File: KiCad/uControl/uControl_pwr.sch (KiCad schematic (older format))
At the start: 30 parts, among them P10 V_IN, P12 UUSB_B, Q1 FDN340P, U1 LP2985-33DBVR, U3 NCP1117ST50T3G, U5 LM358N

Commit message: uControl schematic in progress
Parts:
- removed C15: 1n, c_0805, symbol C
- removed D7: SMBJ5.0CA-TR, diode-DO214AA, symbol DIODE_TRANSIL
- removed F1: nanoSMDC110F, f_1206, symbol FUSE
- removed P12: UUSB_B, USB_B_Micro, symbol UUSB_B
- removed R14: 0E, r_0805, symbol R
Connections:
- net labels removed: USB_IN
- wire segments 89 -> 73
- no-connect marks 3 -> 0
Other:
- note removed: "Bi-directional\nclamping Diode, 5V"
- note removed: "If using Micro USB -B socket, \nDO NOT INSTALL :\nP10, D5, U3\nAND INSTALL\nResistor R14 across pins 2 and 3 of U3\n\nIf using Barrel Socket,\nDO NOT INSTALL :\nP12, F1, D7, C15, R14"
- note removed: "Micro USB-B POWER SOCKET"
- note removed: "Polyswitch resettable fuse\n1.1A Hold, 2.2A Trip 8V max."
- note removed: "TE - 1981568-1\nor\nFCI - 10118193-0001LF"
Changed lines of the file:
@@
-EESchema Schematic File Version 2  date 11/29/2012 6:28:02 PM
+EESchema Schematic File Version 2  date 11/30/2012 11:17:28 AM
 LIBS:uControl
 LIBS:Conn-raspberry
@@
 Sheet 3 5
 Title "uControl"
-Date "29 nov 2012"
+Date "30 nov 2012"
 Rev "1"
 Comp "WyoLum"
@@
 $EndDescr
 Wire Wire Line
-	3575 3925 3575 3400
-Wire Wire Line
-	3575 3400 3300 3400
+	3575 3700 3575 3925
 Wire Notes Line
 	7100 3250 7100 4700
@@
 	7250 4125 7250 4075
 Wire Wire Line
-	7550 4525 7550 4575
+	7550 4575 7550 4525
 Wire Wire Line
 	7550 4575 7250 4575
@@
 Connection ~ 5700 7425
 Wire Wire Line
-	6475 7375 6475 7425
+	6475 7425 6475 7375
 Connection ~ 6350 6400
 Wire Wire Line
-	6475 6425 6475 6400
-Wire Wire Line
-	6475 6400 6300 6400
+	6475 6400 6475 6425
+Wire Wire Line
+	6300 6400 6475 6400
 Connection ~ 5700 5975
 Wire Wire Line
@@
 Wire Notes Line
 	600  5500 600  3250
-Connection ~ 1550 2550
-Wire Wire Line
-	1550 2550 1350 2550
 Connection ~ 5625 5300
 Wire Wire Line
 	5625 5300 5625 5150
-Connection ~ 1550 2200
-Wire Wire Line
-	1550 2200 1350 2200
-Connection ~ 1550 1900
-Wire Wire Line
-	1350 1900 1550 1900
-Wire Wire Line
-	3100 1550 3100 1825
-Connection ~ 3550 1550
-Wire Wire Line
-	3750 1550 1350 1550
-Connection ~ 3100 1550
-Wire Wire Line
-	3550 1550 3550 1450
-Wire Wire Line
-	1350 950  2150 950
 Wire Wire Line
 	7150 6850 7150 6775
@@
 	7425 6775 7425 6725
 Wire Wire Line
-	4150 6275 4150 4375
+	4150 4375 4150 6275
 Wire Wire Line
 	7450 6100 7450 6250
@@
 	2900 7450 2900 7225
 Wire Wire Line
-	4150 4375 4675 4375
+	4675 4375 4150 4375
 Connection ~ 4625 4375
 Wire Wire Line
-	4675 4525 4625 4525
+	4625 4525 4675 4525
 Wire Wire Line
 	1775 5925 3650 5925
@@
 	3025 4250 3025 4350
 Wire Wire Line
-	6400 5300 1800 5300
+	1800 5300 6400 5300
 Connection ~ 1800 3900
 Wire Wire Line
@@
 Connection ~ 4625 5300
 Wire Wire Line
-	2450 4250 2450 4350
+	2450 4350 2450 4250
 Wire Wire Line
 	2450 4350 3850 4350
 Connection ~ 6050 5300
 Wire Wire Line
-	4625 4525 4625 3550
+	4625 3550 4625 4525
 Wire Wire Line
 	3850 3700 3850 3750
@@
 	4900 5975 4900 6975
 Wire Wire Line
-	3550 1050 3550 950
-Connection ~ 3100 950
-Connection ~ 3550 950
-Wire Wire Line
-	3750 950  2850 950
-Wire Wire Line
-	1350 1750 1550 1750
-Wire Wire Line
-	1550 1750 1550 2800
-Wire Wire Line
-	1550 2050 1350 2050
-Connection ~ 1550 2050
-Wire Wire Line
 	5475 4675 5625 4675
 Wire Wire Line
 	5625 4675 5625 4750
-Wire Wire Line
-	1550 2400 1350 2400
-Connection ~ 1550 2400
-Wire Notes Line
-	3950 2950 3950 650
-Wire Notes Line
-	3950 2950 600  2950
-Wire Notes Line
-	600  2950 600  650
-Wire Notes Line
-	600  650  3950 650
 Wire Notes Line
 	4350 5800 600  5800
@@
 	6350 6725 6350 6400
 Wire Wire Line
-	4900 7375 4900 7425
+	4900 7425 4900 7375
 Wire Wire Line
 	6475 6925 6475 6975
 Wire Wire Line
-	4900 7425 6475 7425
+	6475 7425 4900 7425
 Wire Notes Line
 	6725 5800 4600 5800
@@
 Wire Notes Line
 	600  3250 6725 3250
-Wire Wire Line
-	2800 3400 2575 3400
-Wire Wire Line
-	2575 3400 2575 3700
-Connection ~ 2575 3700
-$Comp
-L R R14
-U 1 1 50137293
-P 3050 3400
-F 0 "R14" V 3130 3400 50  0000 C CNN
-F 1 "0E" V 3050 3400 50  0000 C CNN
-F 2 "r_0805" H 3050 3400 60  0001 C CNN
-	1    3050 3400
-	0    -1   -1   0
-$EndComp
-NoConn ~ 1350 1250
-NoConn ~ 1350 1100
 $Comp
 L R R5
@@
 $EndComp
 $Comp
-L GND #PWR14
+L GND #PWR05
 U 1 1 4FE44ABC
 P 7400 4625
-F 0 "#PWR14" H 7400 4625 30  0001 C CNN
+F 0 "#PWR05" H 7400 4625 30  0001 C CNN
 F 1 "GND" H 7400 4555 30  0001 C CNN
 	1    7400 4625
@@
 Text Notes 600  3250 0    60   Italic 12
 BARREL POWER SOCKET
-Text Notes 600  650  0    60   Italic 12
-Micro USB-B POWER SOCKET
-$Comp
-L FUSE F1
-U 1 1 4FDCE35C
-P 2500 950
-F 0 "F1" H 2600 950 60  0000 C CNN
-F 1 "nanoSMDC110F" H 2425 1025 40  0000 C CNN
-F 2 "f_1206" H 2500 950 60  0001 C CNN
-	1    2500 950
-	1    0    0    -1
-$EndComp
-Text Notes 4375 1600 0    60   ~ 12
-If using Micro USB -B socket, \nDO NOT INSTALL :\nP10, D5, U3\nAND INSTALL\nResistor R14 across pins 2 and 3 of U3\n\nIf using Barrel Socket,\nDO NOT INSTALL :\nP12, F1, D7, C15, R14
 $Comp
 L C C16
@@
 	-1   0    0    -1
 $EndComp
-Text Notes 625  2725 0    40   ~ 0
-TE - 1981568-1\nor\nFCI - 10118193-0001LF
-Text Notes 2500 1375 0    40   ~ 0
-Bi-directional\nclamping Diode, 5V
-Text Notes 2200 775  0    40   ~ 0
-Polyswitch resettable fuse\n1.1A Hold, 2.2A Trip 8V max.
 Text Label 1450 3700 0    40   ~ 0
 PWR_IN
-Text Label 1500 950  0    40   ~ 0
-USB_IN
-NoConn ~ 1350 1400
-$Comp
-L GND #PWR4
-U 1 1 4FDA1E9F
-P 1550 2800
-F 0 "#PWR4" H 1550 2800 30  0001 C CNN
-F 1 "GND" H 1550 2730 30  0001 C CNN
-	1    1550 2800
-	-1   0    0    -1
-$EndComp
-$Comp
-L GND #PWR6
-U 1 1 4FDA1E91
-P 3100 1825
-F 0 "#PWR6" H 3100 1825 30  0001 C CNN
-F 1 "GND" H 3100 1755 30  0001 C CNN
-	1    3100 1825
-	-1   0    0    -1
-$EndComp
-Text Label 3750 1550 0    40   ~ 0
-GND
-Text Label 3750 950  0    40   ~ 0
-5V0
-$Comp
-L C C15
-U 1 1 4FDA1E4C
-P 3550 1250
-F 0 "C15" H 3575 1325 50  0000 L CNN
-F 1 "1n" H 3575 1175 50  0000 L CNN
-F 2 "c_0805" H 3550 1250 60  0001 C CNN
-	1    3550 1250
-	-1   0    0    -1
-$EndComp
-$Comp
-L DIODE_TRANSIL D7
-U 1 1 4FDA1DDC
-P 3100 1250
-F 0 "D7" H 3250 1300 60  0000 C CNN
-F 1 "SMBJ5.0CA-TR" H 2725 1225 40  0000 C CNN
-F 2 "diode-DO214AA" H 3100 1750 60  0001 C CNN
-	1    3100 1250
-	1    0    0    -1
-$EndComp
-$Comp
-L UUSB_B P12
-U 1 1 4FDA1DB8
-P 1000 1250
-F 0 "P12" H 1000 1800 60  0000 C CNN
-F 1 "UUSB_B" H 1000 1700 60  0000 C CNN
-F 2 "USB_B_Micro" H 1000 1800 60  0001 C CNN
-	1    1000 1250
-	1    0    0    -1
-$EndComp
 Text Label 5700 5925 0    40   ~ 0
 5V0
@@
 5V0
 $Comp
-L +3.3V #PWR11
+L +3.3V #PWR06
 U 1 1 4FC9DF2C
 P 6050 4225
-F 0 "#PWR11" H 6050 4185 30  0001 C CNN
+F 0 "#PWR06" H 6050 4185 30  0001 C CNN
 F 1 "+3.3V" H 6050 4335 30  0000 C CNN
 	1    6050 4225
@@
 GND
 $Comp
-L GND #PWR13
+L GND #PWR07
 U 1 1 4FC9DE68
 P 7150 6850
-F 0 "#PWR13" H 7150 6850 30  0001 C CNN
+F 0 "#PWR07" H 7150 6850 30  0001 C CNN
 F 1 "GND" H 7150 6780 30  0001 C CNN
 	1    7150 6850
@@
 $EndComp
 $Comp
-L PWR_FLAG #FLG4
+L PWR_FLAG #FLG08
 U 1 1 4FC9DE5A
 P 7425 6725
-F 0 "#FLG4" H 7425 6995 30  0001 C CNN
+F 0 "#FLG08" H 7425 6995 30  0001 C CNN
 F 1 "PWR_FLAG" H 7425 6955 30  0000 C CNN
 	1    7425 6725
@@
 $EndComp
 $Comp
-L PWR_FLAG #FLG2
+L PWR_FLAG #FLG09
 U 1 1 4FC9DE21
 P 1725 3600
-F 0 "#FLG2" H 1725 3870 30  0001 C CNN
+F 0 "#FLG09" H 1725 3870 30  0001 C CNN
 F 1 "PWR_FLAG" H 1725 3830 30  0000 C CNN
 	1    1725 3600
@@
 $EndComp
 $Comp
-L PWR_FLAG #FLG3
+L PWR_FLAG #FLG010
 U 1 1 4FC9DC94
 P 2450 3600
-F 0 "#FLG3" H 2450 3870 30  0001 C CNN
+F 0 "#FLG010" H 2450 3870 30  0001 C CNN
 F 1 "PWR_FLAG" H 2450 3830 30  0000 C CNN
 	1    2450 3600
@@
 3V3
 $Comp
-L PWR_FLAG #FLG5
+L PWR_FLAG #FLG011
 U 1 1 4FC9DB12
 P 7450 6100
-F 0 "#FLG5" H 7450 6370 30  0001 C CNN
+F 0 "#FLG011" H 7450 6370 30  0001 C CNN
 F 1 "PWR_FLAG" H 7450 6330 30  0000 C CNN
 	1    7450 6100
@@
 $EndComp
 $Comp
-L +3.3V #PWR12
+L +3.3V #PWR012
 U 1 1 4FC9DB0D
 P 7150 6100
-F 0 "#PWR12" H 7150 6060 30  0001 C CNN
+F 0 "#PWR012" H 7150 6060 30  0001 C CNN
 F 1 "+3.3V" H 7150 6210 30  0000 C CNN
 	1    7150 6100
@@
 $EndComp
 $Comp
-L GND #PWR10
+L GND #PWR013
 U 1 1 4FC621D3
 P 5700 7475
-F 0 "#PWR10" H 5700 7475 30  0001 C CNN
+F 0 "#PWR013" H 5700 7475 30  0001 C CNN
 F 1 "GND" H 5700 7405 30  0001 C CNN
 	1    5700 7475
@@
 $EndComp
 $Comp
-L GND #PWR5
+L GND #PWR014
 U 1 1 4FC62001
 P 2900 7450
-F 0 "#PWR5" H 2900 7450 30  0001 C CNN
+F 0 "#PWR014" H 2900 7450 30  0001 C CNN
 F 1 "GND" H 2900 7380 30  0001 C CNN
 	1    2900 7450
@@
 5V0
 $Comp
-L +5V #PWR8
+L +5V #PWR015
 U 1 1 4FC61A10
 P 4625 3550
-F 0 "#PWR8" H 4625 3640 20  0001 C CNN
+F 0 "#PWR015" H 4625 3640 20  0001 C CNN
 F 1 "+5V" H 4625 3640 30  0000 C CNN
 	1    4625 3550
@@
 $EndComp
 $Comp
-L GND #PWR9
+L GND #PWR016
 U 1 1 4FC61A0D
 P 4625 5400
-F 0 "#PWR9" H 4625 5400 30  0001 C CNN
+F 0 "#PWR016" H 4625 5400 30  0001 C CNN
 F 1 "GND" H 4625 5330 30  0001 C CNN
 	1    4625 5400
@@
 $EndComp
 $Comp
-L GND #PWR7
+L GND #PWR017
 U 1 1 4FC61A09
 P 3575 4450
-F 0 "#PWR7" H 3575 4450 30  0001 C CNN
+F 0 "#PWR017" H 3575 4450 30  0001 C CNN
 F 1 "GND" H 3575 4380 30  0001 C CNN
 	1    3575 4450

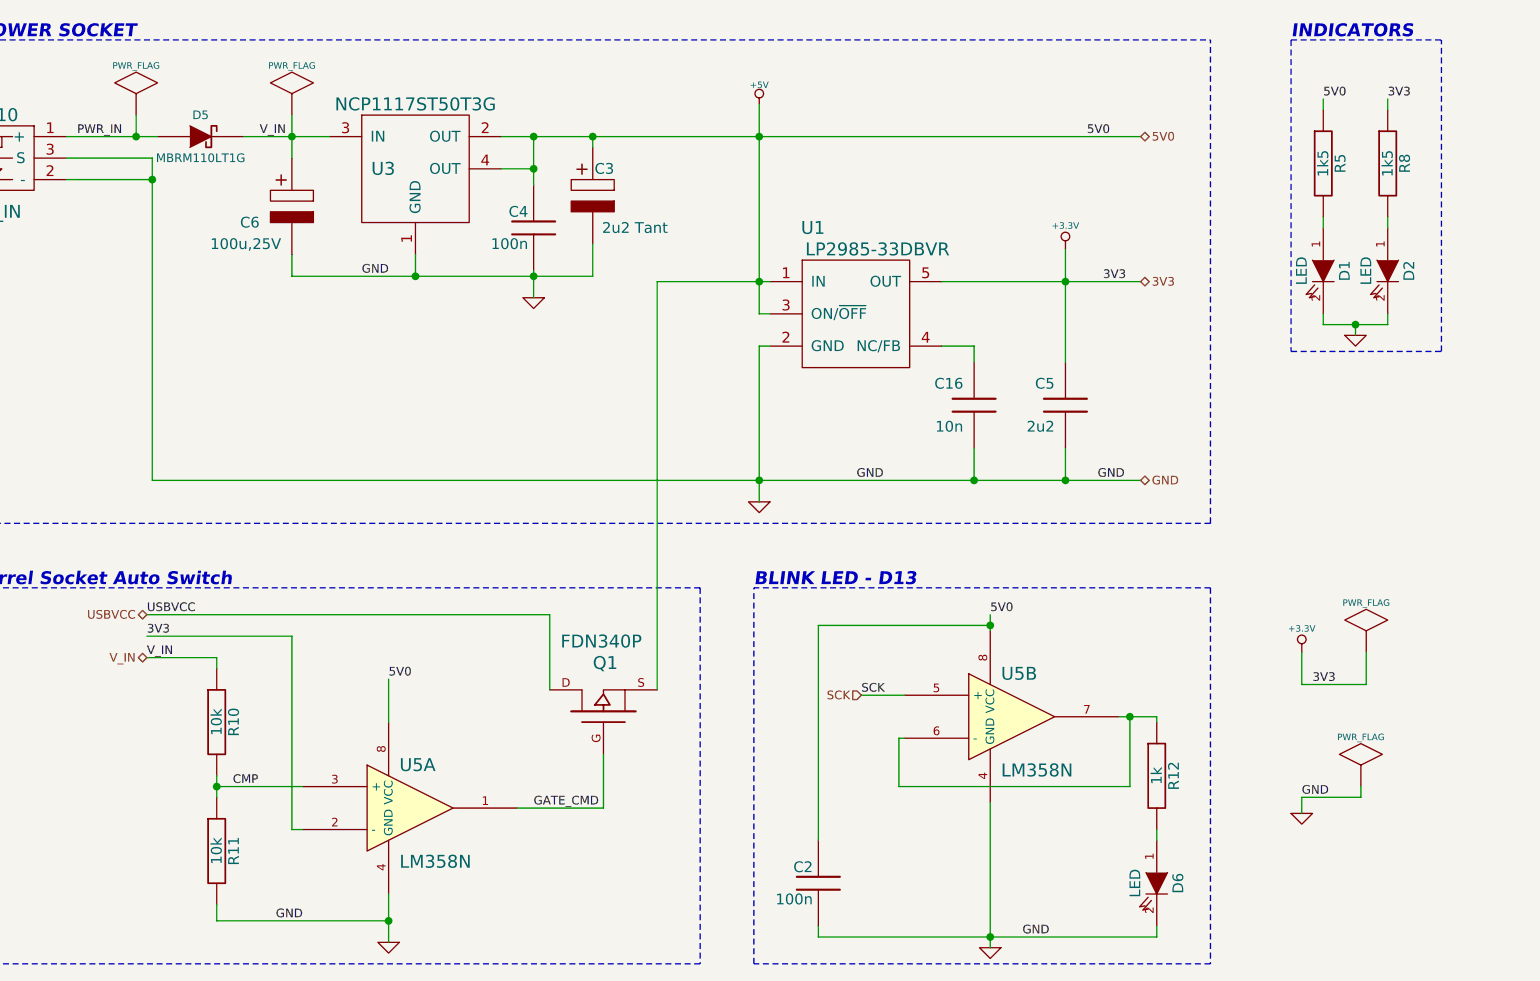
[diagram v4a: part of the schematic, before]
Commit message: uControl : added Temp and Pulse sensors. P/N's for Diodes, Transistor etc.
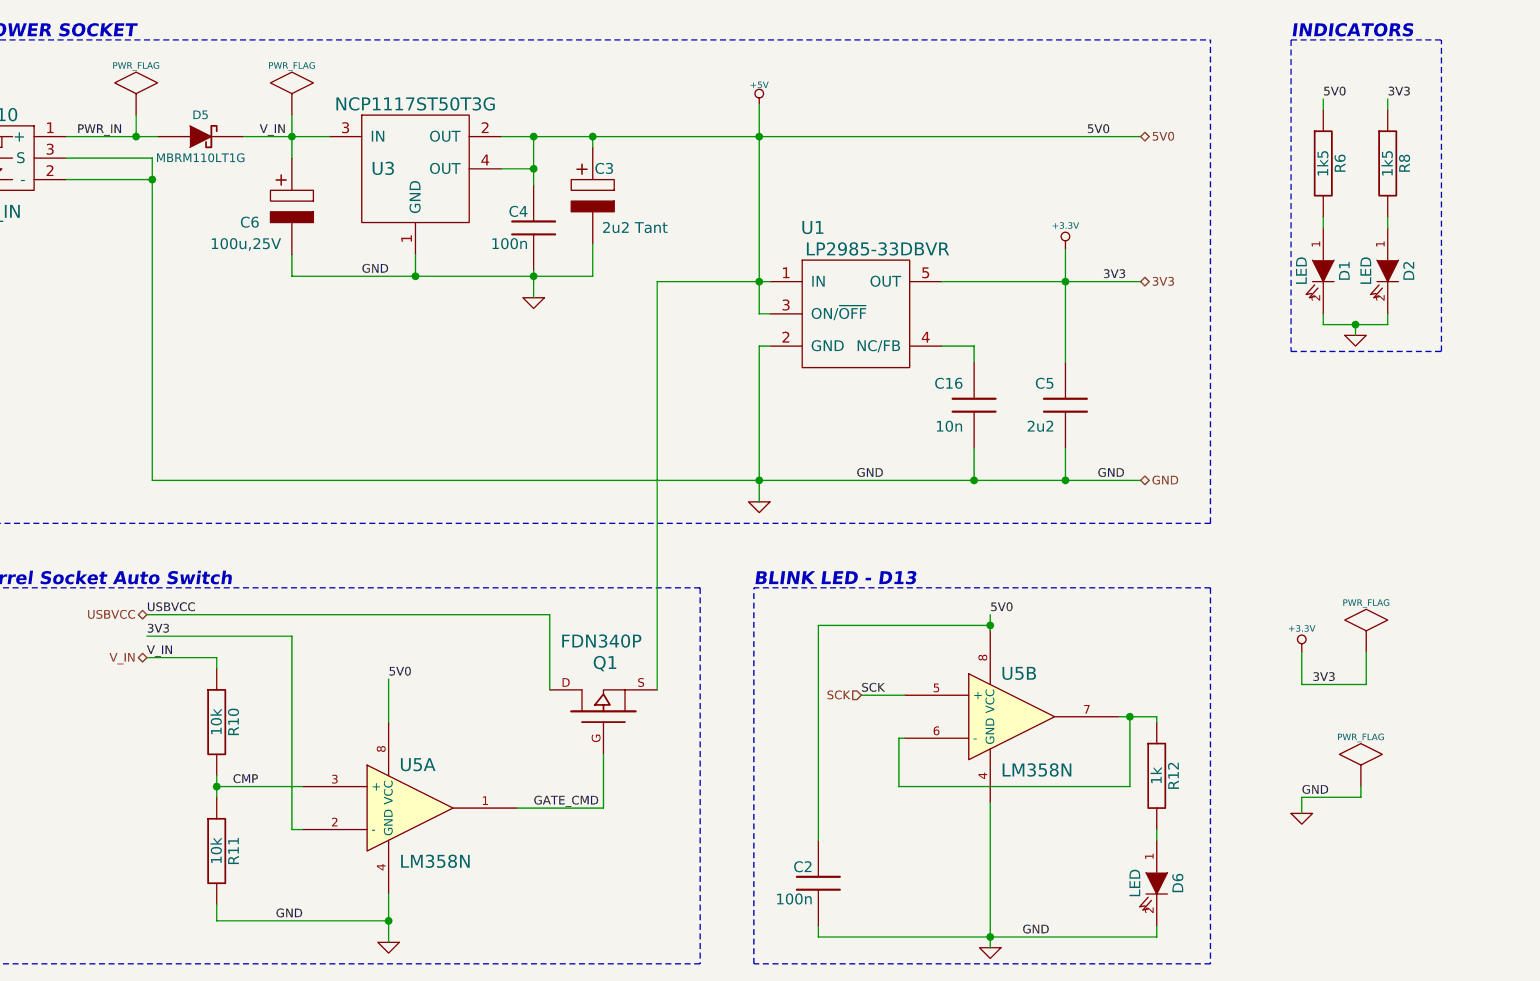
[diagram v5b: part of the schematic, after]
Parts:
- renumbered R5 to R6
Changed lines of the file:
@@
-EESchema Schematic File Version 2  date 12/1/2012 2:57:47 PM
+EESchema Schematic File Version 2  date Sunday 02 December 2012 02:01:49 AM IST
 LIBS:uControl
 LIBS:Conn-raspberry
@@
 	7250 4125 7250 4075
 Wire Wire Line
-	7550 4575 7550 4525
+	7550 4525 7550 4575
 Wire Wire Line
 	7550 4575 7250 4575
@@
 Connection ~ 5700 7425
 Wire Wire Line
-	6475 7425 6475 7375
+	6475 7375 6475 7425
 Connection ~ 6350 6400
 Wire Wire Line
-	6475 6400 6475 6425
-Wire Wire Line
-	6300 6400 6475 6400
+	6475 6425 6475 6400
+Wire Wire Line
+	6475 6400 6300 6400
 Connection ~ 5700 5975
 Wire Wire Line
@@
 	7425 6775 7425 6725
 Wire Wire Line
-	4150 4375 4150 6275
+	4150 6275 4150 4375
 Wire Wire Line
 	7450 6100 7450 6250
@@
 	2900 7450 2900 7225
 Wire Wire Line
-	4675 4375 4150 4375
+	4150 4375 4675 4375
 Connection ~ 4625 4375
 Wire Wire Line
-	4625 4525 4675 4525
+	4675 4525 4625 4525
 Wire Wire Line
 	1775 5925 3650 5925
@@
 	3025 4250 3025 4350
 Wire Wire Line
-	1800 5300 6400 5300
+	6400 5300 1800 5300
 Connection ~ 1800 3900
 Wire Wire Line
@@
 Connection ~ 4625 5300
 Wire Wire Line
-	2450 4350 2450 4250
+	2450 4250 2450 4350
 Wire Wire Line
 	2450 4350 3850 4350
 Connection ~ 6050 5300
 Wire Wire Line
-	4625 3550 4625 4525
+	4625 4525 4625 3550
 Wire Wire Line
 	3850 3700 3850 3750
@@
 	6350 6725 6350 6400
 Wire Wire Line
-	4900 7425 4900 7375
+	4900 7375 4900 7425
 Wire Wire Line
 	6475 6925 6475 6975
 Wire Wire Line
-	6475 7425 4900 7425
+	4900 7425 6475 7425
 Wire Notes Line
 	6725 5800 4600 5800
@@
 	600  3250 6725 3250
 $Comp
-L R R5
+L R R6
 U 1 1 4FE44ABE
 P 7250 3825
-F 0 "R5" V 7330 3825 50  0000 C CNN
+F 0 "R6" V 7330 3825 50  0000 C CNN
 F 1 "1k5" V 7250 3825 50  0000 C CNN
 F 2 "r_0805" H 7250 3825 60  0001 C CNN

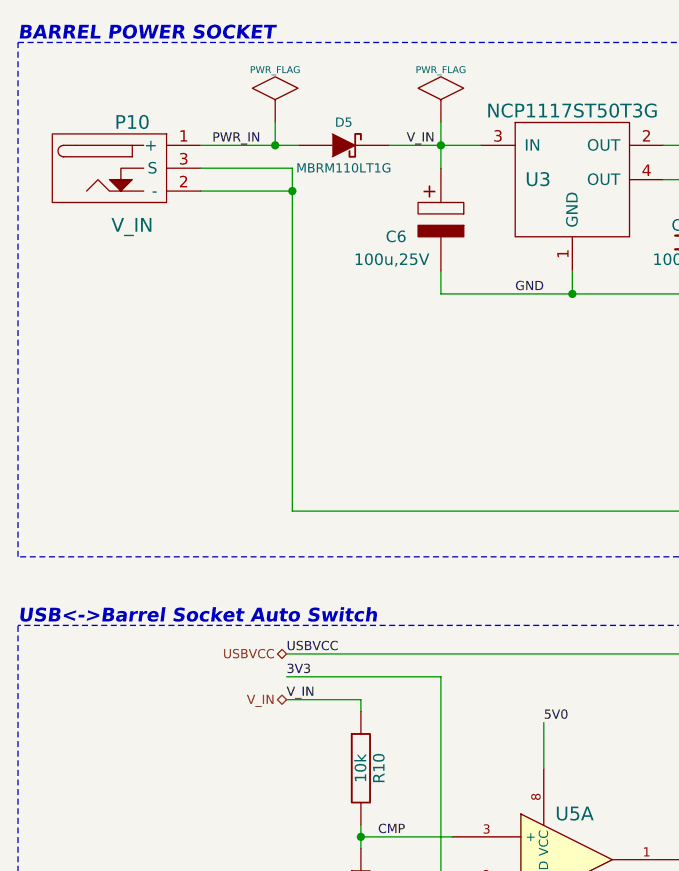
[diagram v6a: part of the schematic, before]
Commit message: uControl schematic work in progress. Added #2 Pr Sensor. Renamed V_In to 12V
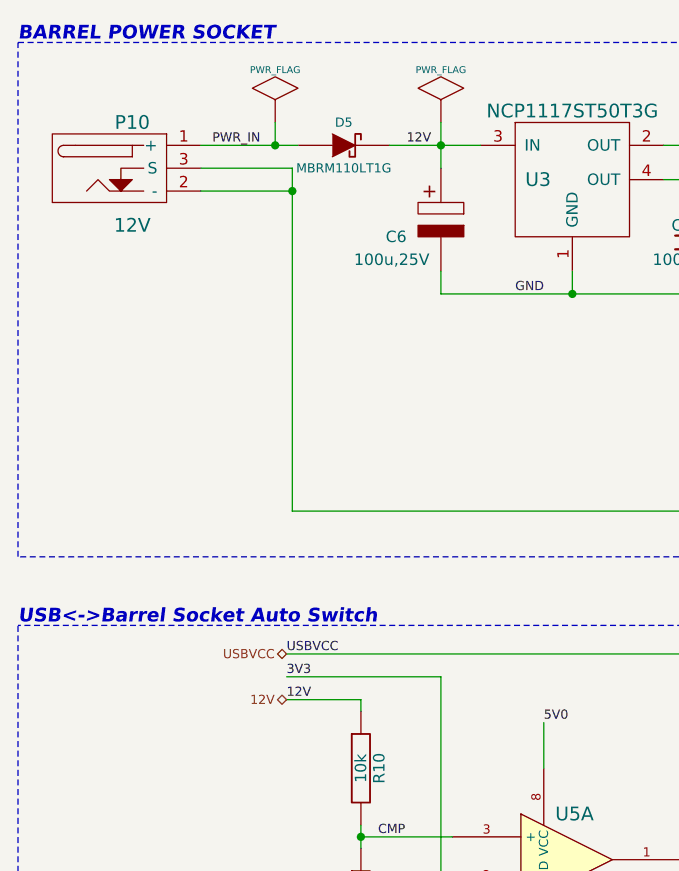
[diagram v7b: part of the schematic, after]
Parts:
- P10: value V_IN -> 12V
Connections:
- net V_IN renamed 12V
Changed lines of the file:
@@
-EESchema Schematic File Version 2  date Sunday 02 December 2012 11:21:38 PM IST
+EESchema Schematic File Version 2  date 12/5/2012 11:54:40 AM
 LIBS:uControl
 LIBS:Conn-raspberry
@@
 Sheet 3 5
 Title "uControl"
-Date "2 dec 2012"
+Date "5 dec 2012"
 Rev "1"
 Comp "WyoLum"
@@
 $EndComp
 Text HLabel 1775 6125 0    40   BiDi ~ 0
-V_IN
+12V
 Text HLabel 1775 5925 0    40   BiDi ~ 0
 USBVCC
@@
 $EndComp
 Text Label 1775 6125 0    40   ~ 0
-V_IN
+12V
 Text Label 2175 6725 0    40   ~ 0
 CMP
@@
 $EndComp
 Text Label 2300 3700 0    40   ~ 0
-V_IN
+12V
 $Comp
 L NCP1117ST50T3G U3
@@
 P 1100 3800
 F 0 "P10" H 1100 4000 60  0000 C CNN
-F 1 "V_IN" H 1100 3550 60  0000 C CNN
+F 1 "12V" H 1100 3550 60  0000 C CNN
 F 2 "JACK_ALIM" H 1100 3800 60  0001 C CNN
 	1    1100 3800

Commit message: uControl some minor edits to schematic
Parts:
- removed C2: 100n, c_0805, symbol C
- removed Q1: FDN340P, SOT23-3, symbol MOSFET_P
- removed R10, R11: 10k, r_0805, symbol R
- removed U5: LM358N, SO8E, symbol LM358N
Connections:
- net SCK: now also R12.1
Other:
- note removed: "USB<->Barrel Socket Auto Switch"
